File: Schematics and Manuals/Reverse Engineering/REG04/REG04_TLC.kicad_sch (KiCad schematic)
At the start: 150 parts, among them J1 Conn_01x02_Pin, J10 Conn_01x02_Pin, J11 Conn_01x02_Pin, J12 Conn_01x02_Pin, J13 Conn_01x02_Pin, J14 Conn_01x02_Pin, J15 Conn_01x02_Pin, J16 Conn_01x02_Pin, J17 Conn_01x02_Pin, J18 Conn_01x02_Pin, J19 Conn_01x02_Pin, J2 Conn_01x02_Pin, J20 Conn_01x02_Pin, J21 Conn_01x02_Pin, J22 Conn_01x02_Pin, J23 Conn_01x02_Pin, J24 Conn_01x02_Pin, J25 Conn_01x02_Pin, J26 Conn_01x02_Pin, J27 Conn_01x02_Pin, J28 Conn_01x02_Pin, J29 Conn_01x02_Pin, J3 Conn_01x02_Pin, J30 Conn_01x02_Pin, J31 Conn_01x02_Pin, J32 Conn_01x02_Pin, J33 Conn_01x02_Pin, J34 Conn_01x02_Pin, J35 Conn_01x02_Pin, J36 Conn_01x02_Pin, J37 Conn_01x02_Pin, J38 Conn_01x02_Pin, J39 Conn_01x02_Pin, J4 Conn_01x02_Pin, J40 Conn_01x02_Pin, J5 Conn_01x02_Pin, J6 Conn_01x02_Pin, J7 Conn_01x02_Pin, J8 Conn_01x02_Pin, J9 Conn_01x02_Pin, Q1 PNP, Q10 PNP, Q11 PNP, Q12 PNP, Q13 PNP, Q14 PNP, Q15 PNP, Q16 PNP, Q2 PNP, Q3 PNP, Q4 PNP, Q5 PNP, Q6 PNP, Q7 PNP, Q8 PNP, Q9 PNP

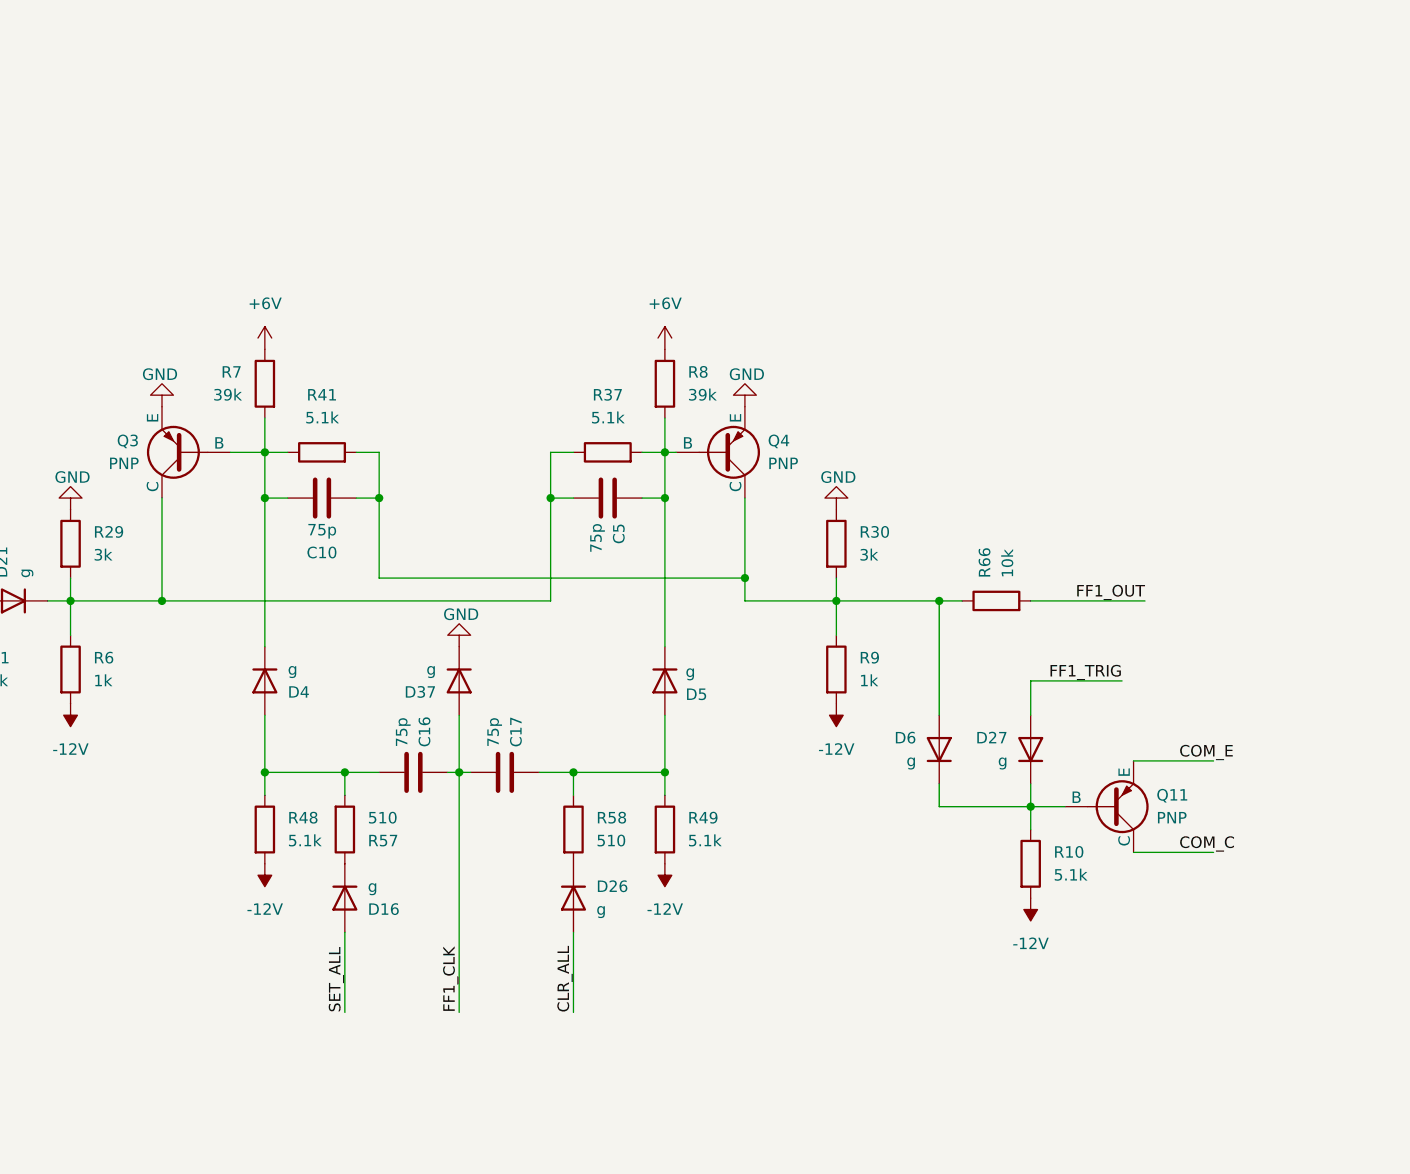
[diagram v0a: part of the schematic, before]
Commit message: another reg04 update, but this is overtaken by bruce and roy
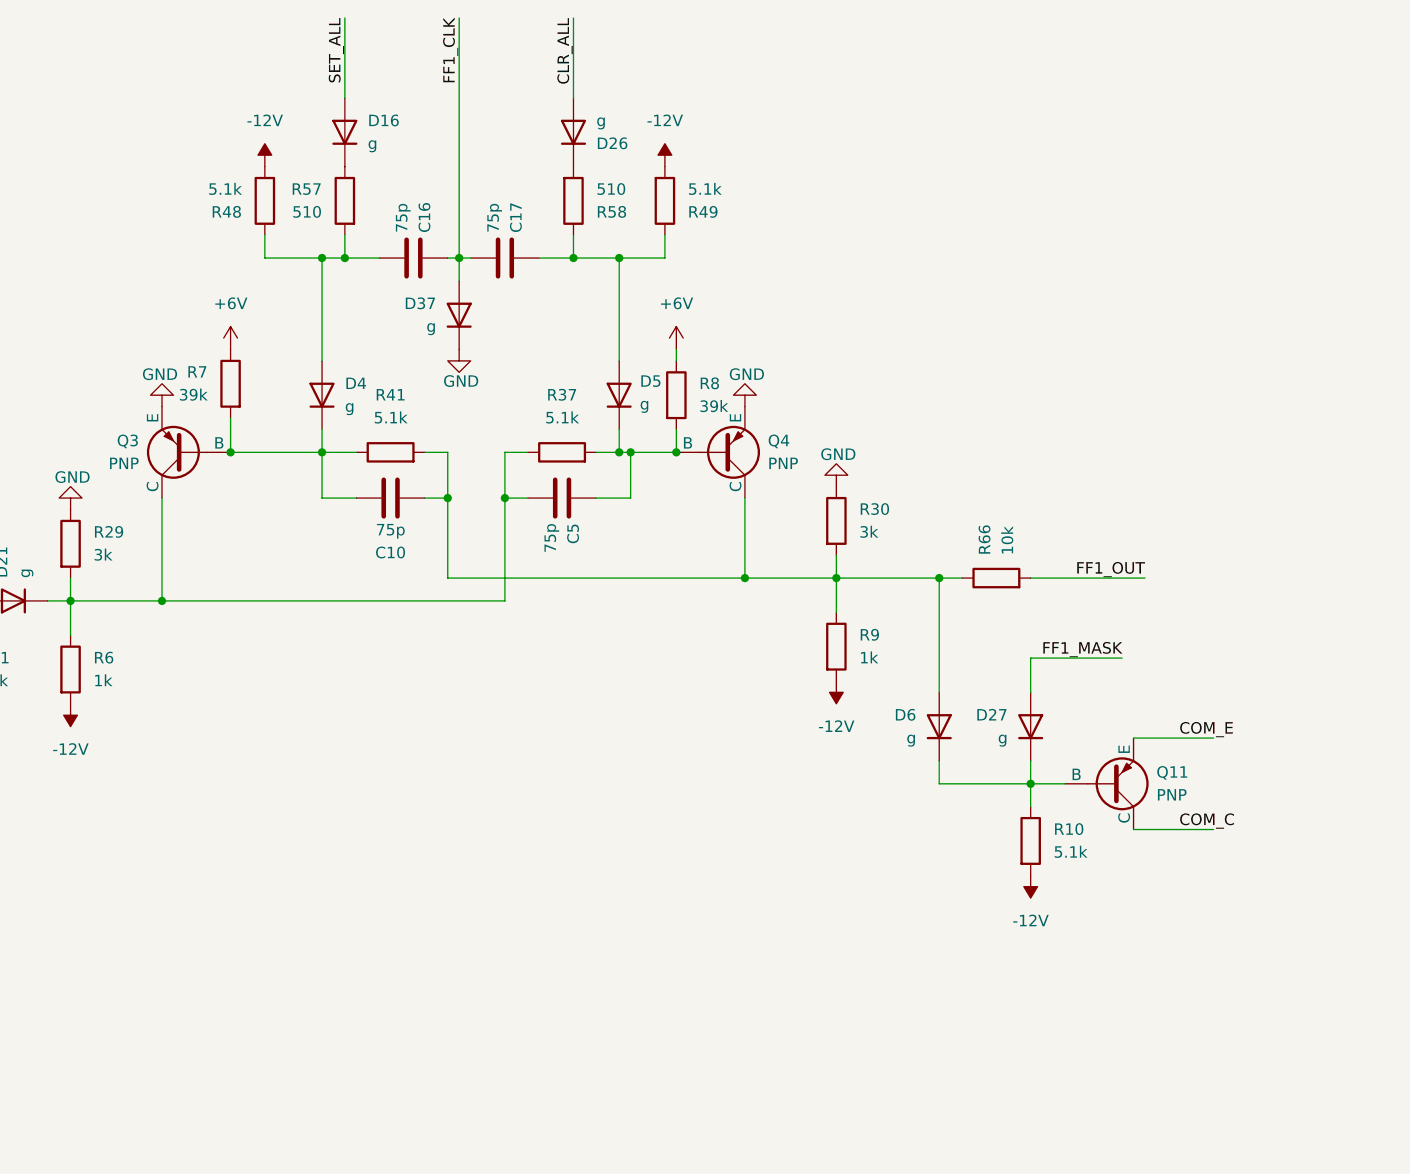
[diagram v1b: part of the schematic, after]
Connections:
- net J22: no longer D27.2 (A)
- new net FF1_MASK: D27.2 (A)
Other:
- moved on the sheet: C10, C16, C17, C5, D16, D26, D27, D37, D4, D5, D6, Q11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
